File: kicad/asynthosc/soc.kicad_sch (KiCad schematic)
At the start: 47 parts, among them J10 Conn_02x07_Odd_Even, J12 Conn_02x04_Odd_Even, J9 Conn_ARM_SWD_TagConnect_TC203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, SW2 SW_Push, U10 W25Q32JVSS, U2 STM32F723VETx, Y1 8MHz, 8pF

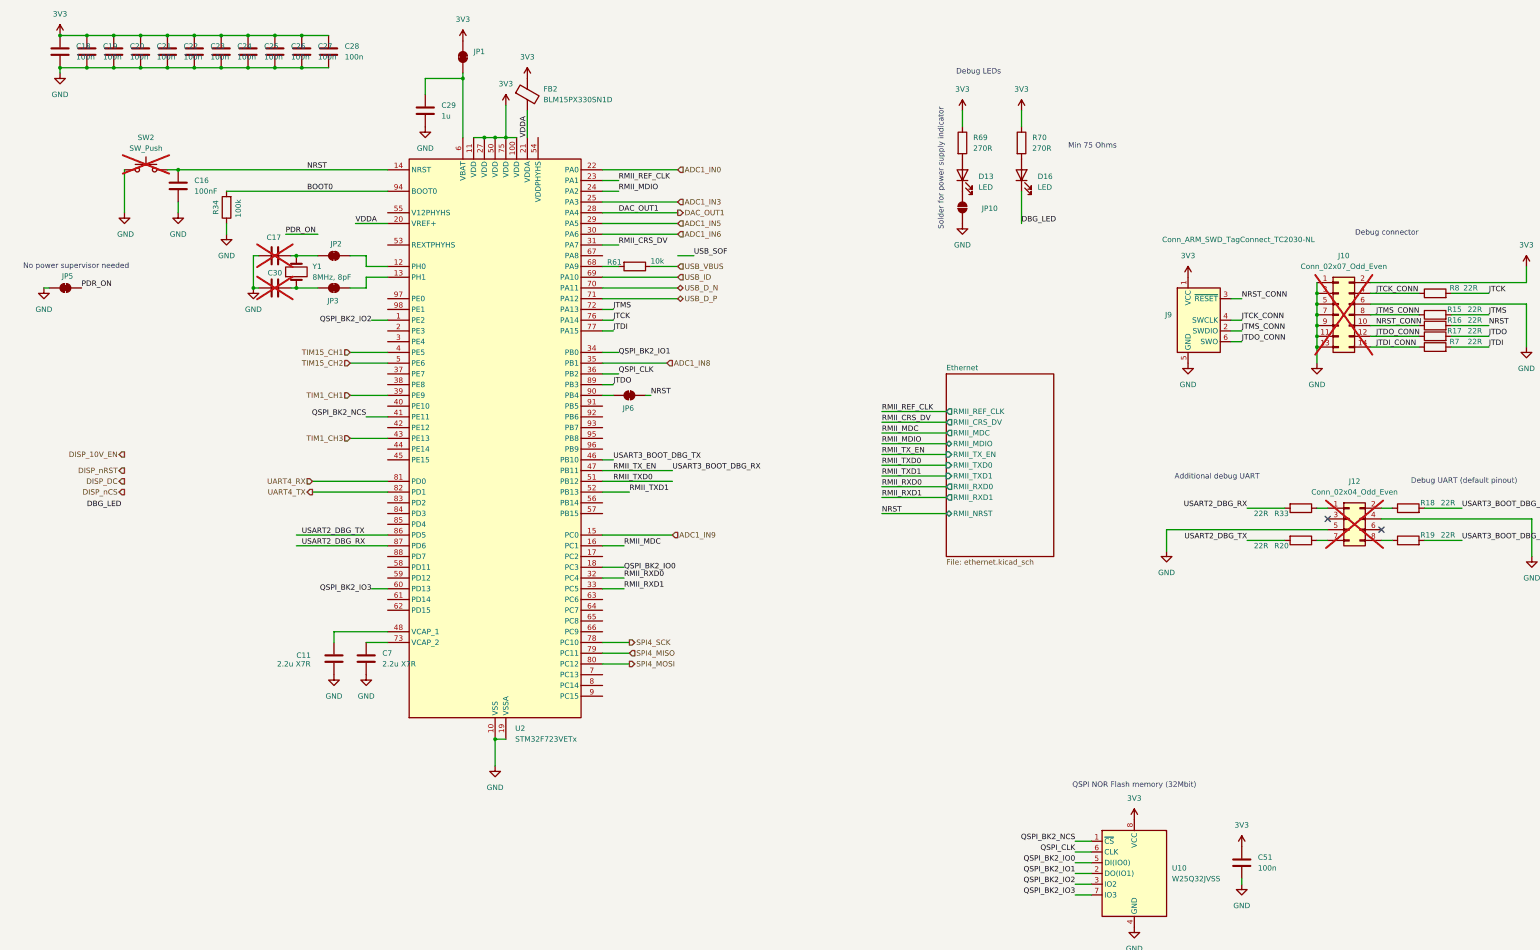
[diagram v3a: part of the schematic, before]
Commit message: bom: update bom for lcsc
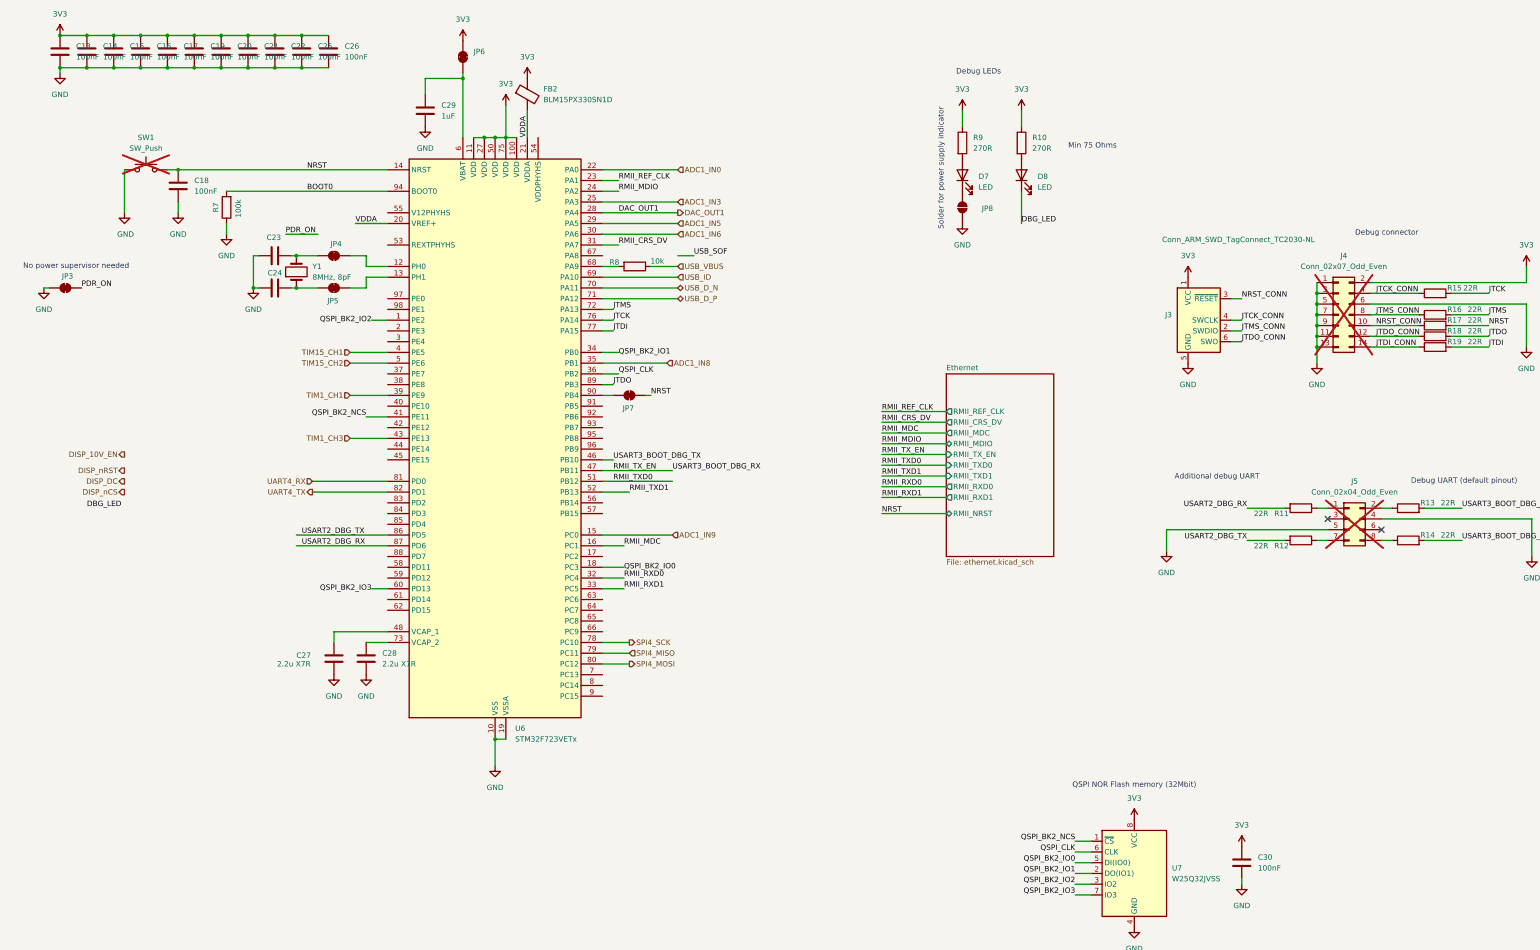
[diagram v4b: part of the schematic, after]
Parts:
- C13: renamed from C18; value 100n -> 100nF
- C14: renamed from C19; value 100n -> 100nF
- C15: renamed from C20; value 100n -> 100nF
- C16: renamed from C21; value 100n -> 100nF
- C17: renamed from C22; value 100n -> 100nF
- C19: renamed from C23; value 100n -> 100nF
- C20: renamed from C24; value 100n -> 100nF
- C21: renamed from C25; value 100n -> 100nF
- C22: renamed from C26; value 100n -> 100nF
- C23: renamed from C17; now fitted
- C24: renamed from C30; now fitted
- C25: renamed from C27; value 100n -> 100nF
- C26: renamed from C28; value 100n -> 100nF
- C29: value 1u -> 1uF
- C30: renamed from C51; value 100n -> 100nF
- J3: renamed from J9; RefNum (none) -> _na_
- J4: renamed from J10; RefNum (none) -> _na_
- J5: renamed from J12; RefNum (none) -> _na_
- JP3: renamed from JP5; RefNum (none) -> _na_
- JP4: renamed from JP2; RefNum (none) -> _na_
- JP5: renamed from JP3; RefNum (none) -> _na_
- JP6: renamed from JP1; RefNum (none) -> _na_
- JP7: renamed from JP6; RefNum (none) -> _na_
- JP8: renamed from JP10; RefNum (none) -> _na_
- R10: renamed from R70; RefNum (none) -> _generic_
- R11: renamed from R33; RefNum (none) -> _generic_
- R12: renamed from R20; RefNum (none) -> _generic_
- R13: renamed from R18; RefNum (none) -> _generic_
- R14: renamed from R19; RefNum (none) -> _generic_
- R15: renamed from R8; RefNum (none) -> _generic_
- R16: renamed from R15; RefNum (none) -> _generic_
- R17: renamed from R16; RefNum (none) -> _generic_
- R18: renamed from R17; RefNum (none) -> _generic_
- R19: renamed from R7; RefNum (none) -> _generic_
- R7: renamed from R34; RefNum (none) -> _generic_
- R8: renamed from R61; RefNum (none) -> _generic_
- R9: renamed from R69; RefNum (none) -> _generic_
- U6: renamed from U2; Manufacturer ST -> STMicroelectronics; RefNum STM32F723VGTx -> STM32H723VGT6
- Y1: footprint Crystal:Crystal_SMD_3225-4Pin_3.2x2.5mm -> asynthosc:Crystal_SMD_3225-2Pin_3.2x2.5mm; Manufacturer (none) -> NDK; RefNum (none) -> NX3225GD-8MHZ-STD-CRA-3
- renumbered C16 to C18, C11 to C27, C7 to C28, D13 to D7, D16 to D8, SW2 to SW1, U10 to U7

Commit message: pcb: placing
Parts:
- removed JP3: SolderJumper_2_Bridged, asynthosc:SolderJumper_0402_1005Metric_Bridged, symbol Jumper:SolderJumper_2_Bridged
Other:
- note removed: "No power supervisor needed"
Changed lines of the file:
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@@
 	(wire
 		(pts
-			(xy 77.47 67.31) (xy 85.09 67.31)
-		)
-		(stroke
-			(width 0)
-			(type default)
-		)
-	)
-	(wire
-		(pts
 			(xy 36.83 27.94) (xy 43.18 27.94)
 		)
@@
 	(wire
 		(pts
-			(xy 20.32 80.01) (xy 21.59 80.01)
-		)
-		(stroke
-			(width 0)
-			(type default)
-		)
-	)
-	(wire
-		(pts
 			(xy 157.48 146.05) (xy 152.4 146.05)
 		)
@@
 		)
 	)
-	(text "No power supervisor needed"
-		(exclude_from_sim no)
-		(at 27.94 74.93 0)
-		(effects
-			(font
-				(size 1.27 1.27)
-			)
-		)
-	)
 	(text "144P: STM32H723ZGTx\n100P: STM32H723VGT6"
 		(exclude_from_sim no)
@@
 		)
 	)
-	(label "PDR_ON"
-		(at 77.47 67.31 0)
-		(fields_autoplaced yes)
-		(effects
-			(font
-				(size 1.27 1.27)
-			)
-			(justify left bottom)
-		)
-	)
 	(label "RMII_CRS_DV"
 		(at 156.21 69.85 0)
@@
 		)
 	)
-	(label "PDR_ON"
-		(at 29.21 80.01 0)
-		(fields_autoplaced yes)
-		(effects
-			(font
-				(size 1.27 1.27)
-			)
-			(justify left bottom)
-		)
-	)
 	(label "JTCK_CONN"
 		(at 303.53 87.63 0)
@@
 					(unit 1)
 				)
-			)
-		)
-	)
-	(symbol
-		(lib_id "power:GND")
-		(at 20.32 80.01 0)
-		(unit 1)
-		(exclude_from_sim no)
-		(in_bom yes)
-		(on_board yes)
-		(dnp no)
-		(fields_autoplaced yes)
-		(property "Reference" "#PWR028"
-			(at 20.32 86.36 0)
-			(effects
-				(font
-					(size 1.27 1.27)
-				)
-				(hide yes)
-			)
-		)
-		(property "Value" "GND"
-			(at 20.32 85.09 0)
-			(effects
-				(font
-					(size 1.27 1.27)
-				)
-			)
-		)
-		(property "Footprint" ""
-			(at 20.32 80.01 0)
-			(effects
-				(font
-					(size 1.27 1.27)
-				)
-				(hide yes)
-			)
-		)
-		(property "Datasheet" ""
-			(at 20.32 80.01 0)
-			(effects
-				(font
-					(size 1.27 1.27)
-				)
-				(hide yes)
-			)
-		)
-		(property "Description" "Power symbol creates a global label with name \"GND\" , ground"
-			(at 20.32 80.01 0)
-			(effects
-				(font
-					(size 1.27 1.27)
-				)
-				(hide yes)
-			)
-		)
-		(pin "1"
-		)
-		(instances
-			(project "asynthosc"
-				(path "/d73e377a-a016-415f-8824-91cc6e4907b9/dee5e89d-6774-4f8d-b6d8-6a859b9e32e8"
-					(reference "#PWR028")
-					(unit 1)
-				)
-			)
-		)
-	)
-	(symbol
-		(lib_id "Jumper:SolderJumper_2_Bridged")
-		(at 25.4 80.01 180)
-		(unit 1)
-		(exclude_from_sim yes)
-		(in_bom no)
-		(on_board yes)
-		(dnp no)
-		(property "Reference" "JP3"
-			(at 25.908 77.216 0)
-			(effects
-				(font
-					(size 1.27 1.27)
-				)
-			)
-		)
-		(property "Value" "SolderJumper_2_Bridged"
-			(at 26.6699 77.47 90)
-			(effects
-				(font
-					(size 1.27 1.27)
-				)
-				(justify right)
-				(hide yes)
-			)
-		)
-		(property "Footprint" "asynthosc:SolderJumper_0402_1005Metric_Bridged"
-			(at 25.4 80.01 0)
-			(effects
-				(font
-					(size 1.27 1.27)
-				)
-				(hide yes)
-			)
-		)
-		(property "Datasheet" "~"
-			(at 25.4 80.01 0)
-			(effects
-				(font
-					(size 1.27 1.27)
-				)
-				(hide yes)
-			)
-		)
-		(property "Description" "Solder Jumper, 2-pole, closed/bridged"
-			(at 25.4 80.01 0)
-			(effects
-				(font
-					(size 1.27 1.27)
-				)
-				(hide yes)
-			)
-		)
-		(property "LCSC" ""
-			(at 25.4 80.01 0)
-			(effects
-				(font
-					(size 1.27 1.27)
-				)
-				(hide yes)
-			)
-		)
-		(property "Manufacturer" ""
-			(at 25.4 80.01 0)
-			(effects
-				(font
-					(size 1.27 1.27)
-				)
-				(hide yes)
-			)
-		)
-		(property "RefNum" "_na_"
-			(at 25.4 80.01 0)
-			(effects
-				(font
-					(size 1.27 1.27)
-				)
-				(hide yes)
-			)
-		)
-		(pin "1"
-		)
-		(pin "2"
-		)
-		(instances
-			(project "asynthosc"
-				(path "/d73e377a-a016-415f-8824-91cc6e4907b9/dee5e89d-6774-4f8d-b6d8-6a859b9e32e8"
-					(reference "JP3")
-					(unit 1)
-				)

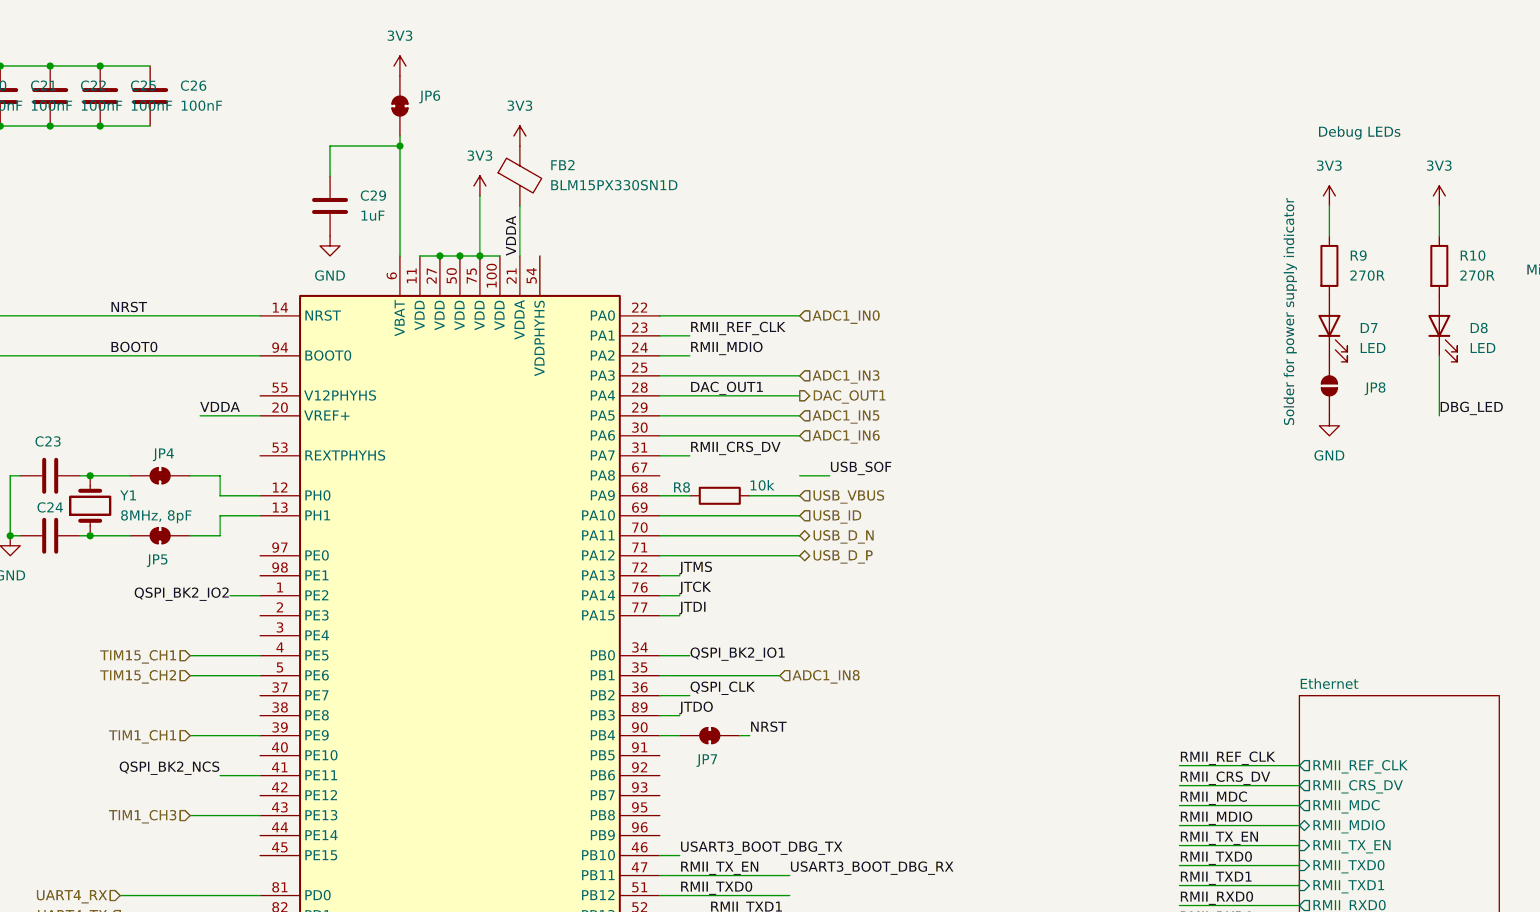
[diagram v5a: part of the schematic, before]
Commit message: pcb: place and change some components for easier routing
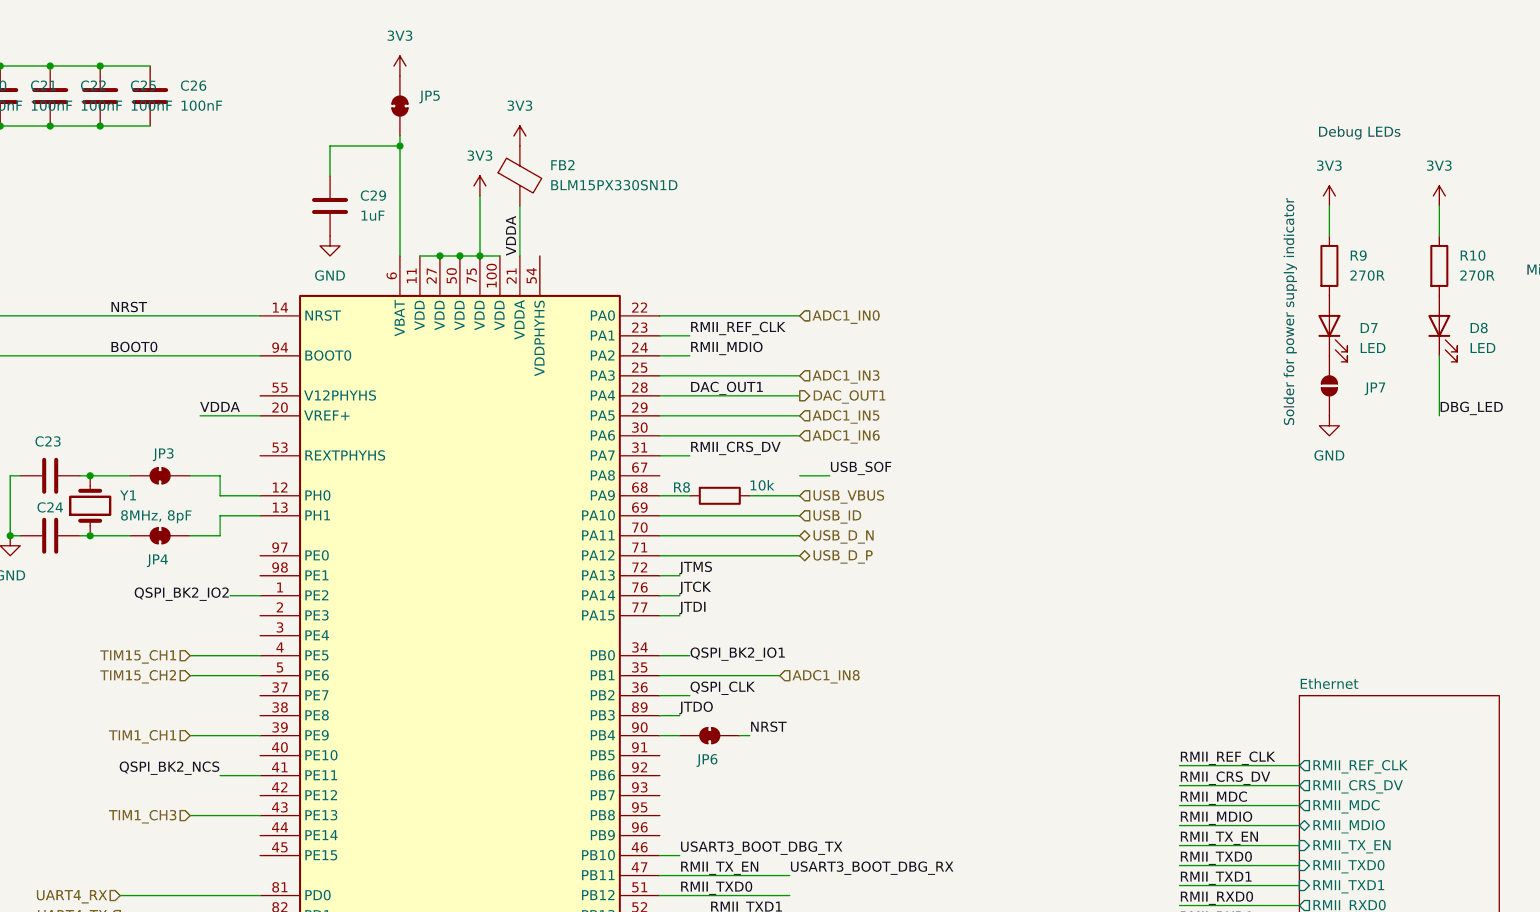
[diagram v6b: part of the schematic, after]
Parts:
- renumbered JP4 to JP3, JP5 to JP4, JP6 to JP5, JP7 to JP6, JP8 to JP7

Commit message: pcb: place and draft route
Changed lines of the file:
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@@
-	(wire
-		(pts
-			(xy 170.18 72.39) (xy 173.99 72.39)
-		)
-		(stroke
-			(width 0)
-			(type default)
-		)
-	)
 	(wire
 		(pts
